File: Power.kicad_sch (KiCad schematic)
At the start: 88 parts, among them Q3 FDMC510P, U32 ZXCT1009F, U33 TPS82150, U34 LT3097, U35 LT8582

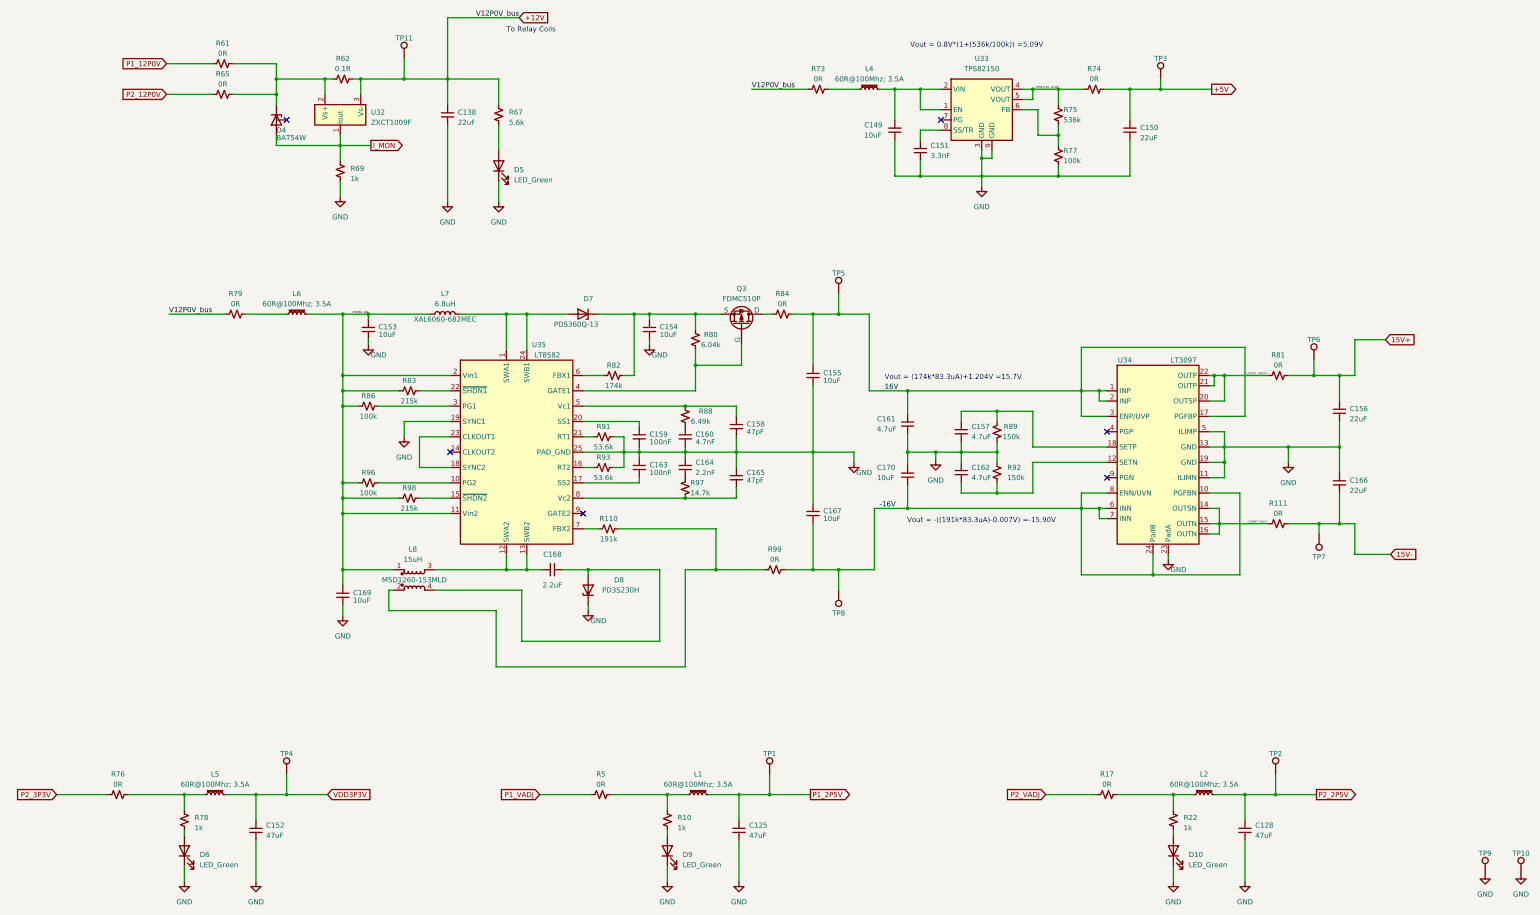
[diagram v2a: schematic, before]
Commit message: Fixed remaining ERC errors and Warnings
No changes affecting copper were made.
At the end of this commits changes all changes from this and the previous two commits were pulled into the PCB.
No changes to the layout occurred and no additional pcb error or warning were made

Detailed Changes:
-Saved the Local Symbol to the project symbol lib and relinked for
  - Q1 & Q2 (looks like symbol was removed from std lib)
  - Max4896 IC's (U14..U23)
  - U32 | ZXCT1009F
  - L8 | MDS1260
  - Q3
  - U33
  - U34 to include thermal pad definitions
  - Mounting holes (Caused a footprint linking error as we linked to a custom footprint)
  - L7 (Caused a footprint linking error as we linked to a custom footprint)
  - P1 & P2 FMC connectors

-Removed Footprint Filter on the following library symbols to clear the footprint linking error
  - DB37 Connectors
  - Relays
  - Mounting Holes
  - U36, U37, D4, L7, L8, U33

-Updated J5 from standard library (no visual change occurred)

-Added Power Flag directives to clear up some warning on various power rails.

-Excluded 5 remaining warnings with comments
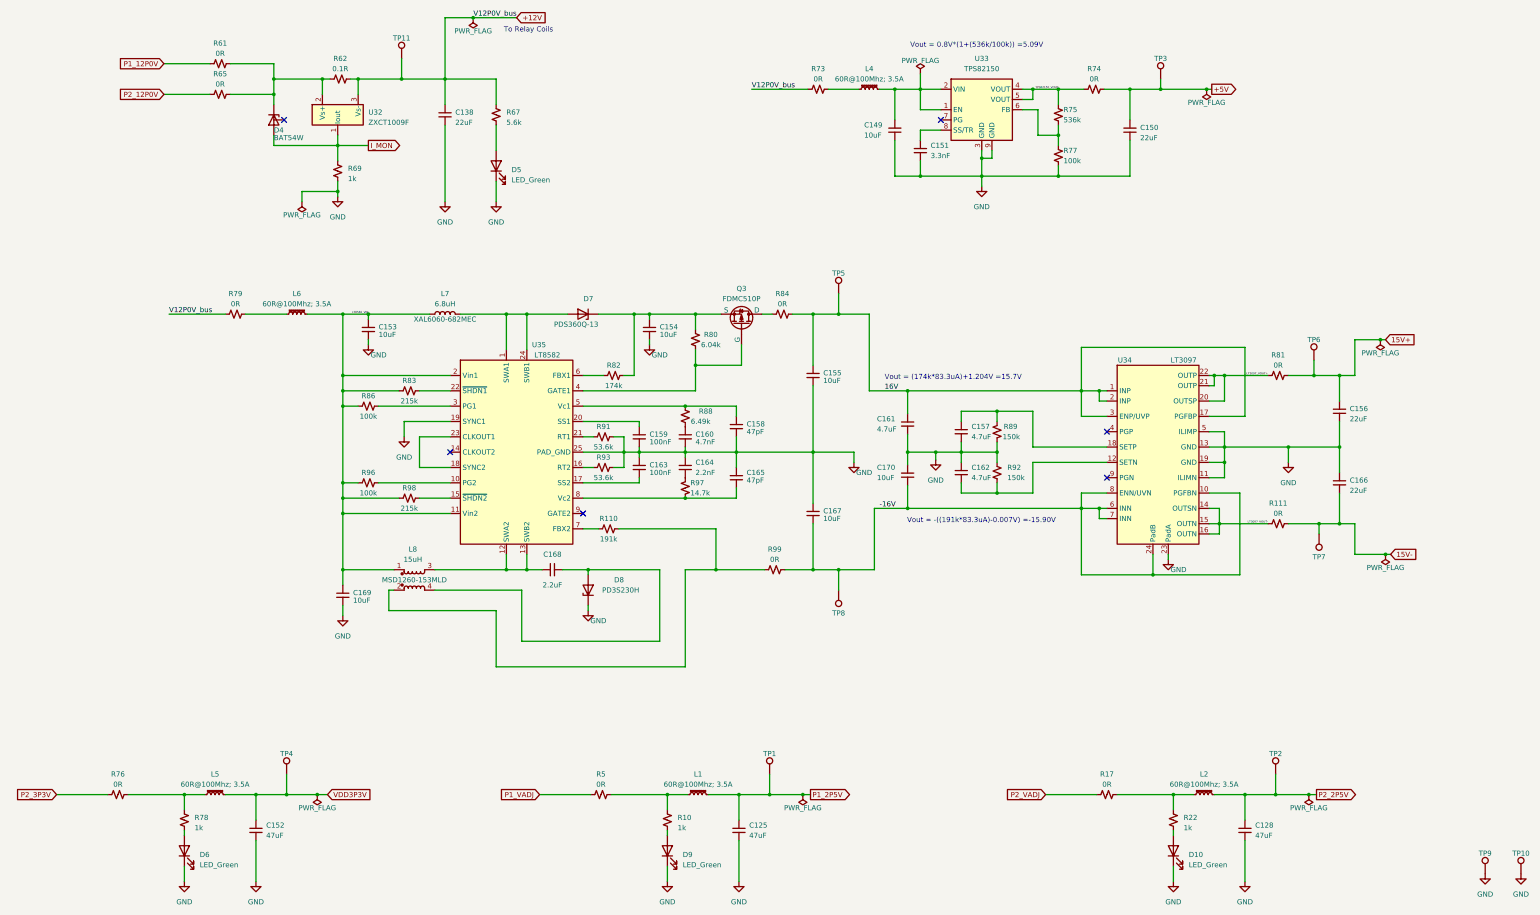
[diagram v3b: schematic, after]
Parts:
- L7: symbol Device:L -> AD7768_Digitizer_SLib:XAL6060
- L8: symbol Device:L_Coupled -> AD7768_Digitizer_SLib:MSD1260
- Q3: symbol Simulation_SPICE:PMOS -> AD7768_Digitizer_SLib:PMOS
- U32: symbol Amplifier_Current:ZXCT1009F -> AD7768_Digitizer_SLib:ZXCT1009F
- U33: symbol Regulator_Switching:TPS82150 -> AD7768_Digitizer_SLib:TPS82150
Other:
- moved on the sheet: C138, D4, D5, R61, R62, R65, R67, R69, TP11, U32

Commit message: Create output job, a couple of fixes
- Created a output job file.
  - This will generate all the output products in a consistant way
  - This was tested OK agianst maunally creating the output objects
- Removed Output Objects for version control
- Removed a Power ERC net object from the CAL EEPROM to fix an ERC error
- Added Explict Manufacturer for the test points for ordering clarity
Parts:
- TP1, TP10, TP11, TP2, TP3, TP4, TP5, TP6, TP7, TP8, TP9: MF (none) -> Keystone Electronics
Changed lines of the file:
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@@
 	(title_block
 		(title "Quartz")
-		(date "2024-03-28")
-		(rev "v1.2.1")
+		(date "2025-04-17")
+		(rev "v1.3")
 		(company "OspreyDCS")
 	)
@@
 			)
 		)
+		(property "MF" "Keystone Electronics"
+			(at 224.79 163.83 0)
+			(effects
+				(font
+					(size 1.27 1.27)
+				)
+				(hide yes)
+			)
+		)
 		(pin "1"
 		)
@@
 			)
 		)
+		(property "MF" "Keystone Electronics"
+			(at 385.445 234.315 0)
+			(effects
+				(font
+					(size 1.27 1.27)
+				)
+				(hide yes)
+			)
+		)
 		(pin "1"
 		)
@@
 			)
 		)
+		(property "MF" "Keystone Electronics"
+			(at 207.645 209.55 0)
+			(effects
+				(font
+					(size 1.27 1.27)
+				)
+				(hide yes)
+			)
+		)
 		(pin "1"
 		)
@@
 			)
 		)
+		(property "MF" "Keystone Electronics"
+			(at 224.79 90.17 0)
+			(effects
+				(font
+					(size 1.27 1.27)
+				)
+				(hide yes)
+			)
+		)
 		(pin "1"
 		)
@@
 			)
 		)
+		(property "MF" "Keystone Electronics"
+			(at 116.205 31.75 0)
+			(effects
+				(font
+					(size 1.27 1.27)
+				)
+				(hide yes)
+			)
+		)
 		(pin "1"
 		)
@@
 			)
 		)
+		(property "MF" "Keystone Electronics"
+			(at 344.17 149.86 0)
+			(effects
+				(font
+					(size 1.27 1.27)
+				)
+				(hide yes)
+			)
+		)
 		(pin "1"
 		)
@@
 			)
 		)
+		(property "MF" "Keystone Electronics"
+			(at 394.335 234.315 0)
+			(effects
+				(font
+					(size 1.27 1.27)
+				)
+				(hide yes)
+			)
+		)
 		(pin "1"
 		)
@@
 			)
 		)
+		(property "MF" "Keystone Electronics"
+			(at 342.9 106.68 0)
+			(effects
+				(font
+					(size 1.27 1.27)
+				)
+				(hide yes)
+			)
+		)
 		(pin "1"
 		)
@@
 			)
 		)
+		(property "MF" "Keystone Electronics"
+			(at 304.8 36.83 0)
+			(effects
+				(font
+					(size 1.27 1.27)
+				)
+				(hide yes)
+			)
+		)
 		(pin "1"
 		)
@@
 			)
 		)
+		(property "MF" "Keystone Electronics"
+			(at 333.375 209.55 0)
+			(effects
+				(font
+					(size 1.27 1.27)
+				)
+				(hide yes)
+			)
+		)
 		(pin "1"
 		)
@@
 			(at 87.63 209.55 0)
 			(effects
+				(font
+					(size 1.27 1.27)
+				)
+				(hide yes)
+			)
+		)
+		(property "MF" "Keystone Electronics"
+			(at 87.63 209.55 0)
+			(effects
